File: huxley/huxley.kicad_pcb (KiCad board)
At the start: 2 copper layers, 2 parts, among them U6 NVT2010PW_118

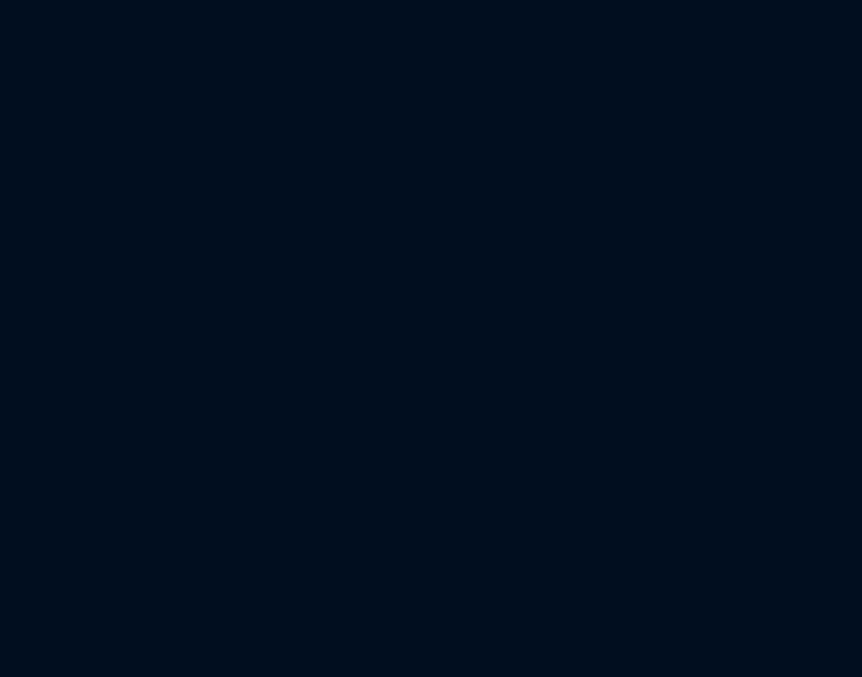
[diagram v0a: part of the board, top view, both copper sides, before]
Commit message: added analog chip schematics and connector footprints
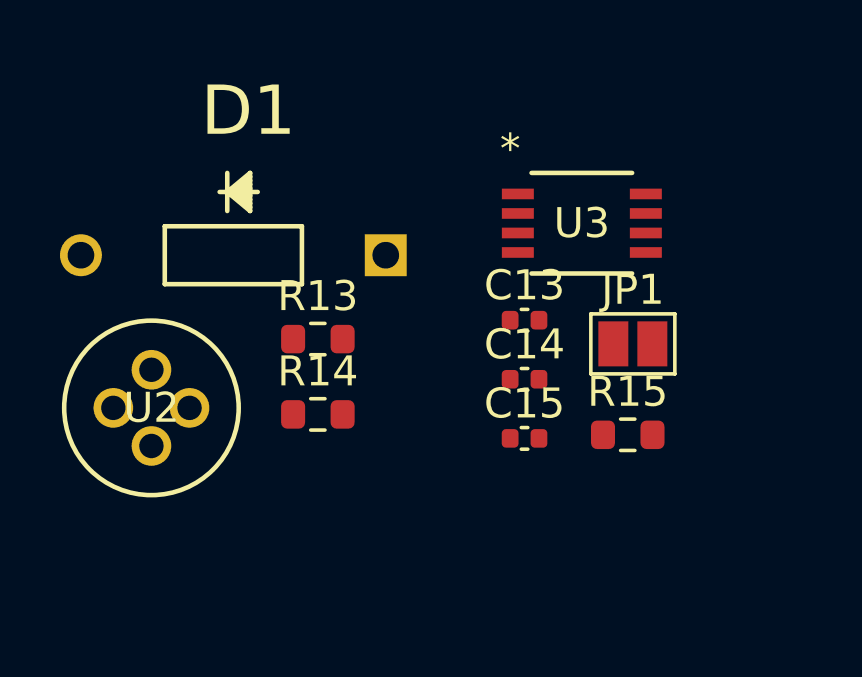
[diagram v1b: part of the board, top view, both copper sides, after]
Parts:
- added C13: 0.1u, Capacitor_SMD:C_0402_1005Metric, F.Cu at (50.2, 36.7)
- added C14: 1n, Capacitor_SMD:C_0402_1005Metric, F.Cu at (50.2, 38.6)
- added C15: 10p, Capacitor_SMD:C_0402_1005Metric, F.Cu at (50.2, 40.6)
- added D1: 1N457, 726_footprints:DIO_1N457, F.Cu at (45.6, 34.5)
- added JP1: Jumper_2_Open, Jumper:SolderJumper-2_P1.3mm_Open_Pad1.0x1.5mm, F.Cu at (53.8, 37.5)
- added R13: 1.59k, Resistor_SMD:R_0603_1608Metric, F.Cu at (43.3, 37.3)
- added R14: 15.9k, Resistor_SMD:R_0603_1608Metric, F.Cu at (43.3, 39.8)
- added R15: 500, Resistor_SMD:R_0603_1608Metric, F.Cu at (53.7, 40.5)
- added U2: LM134H, 726_footprints:lm134, F.Cu at (37.8, 40.9)
- added U3: MAX40201FAUA+, 726_footprints:MAX40201FAUA+, F.Cu at (52.1, 33.4)

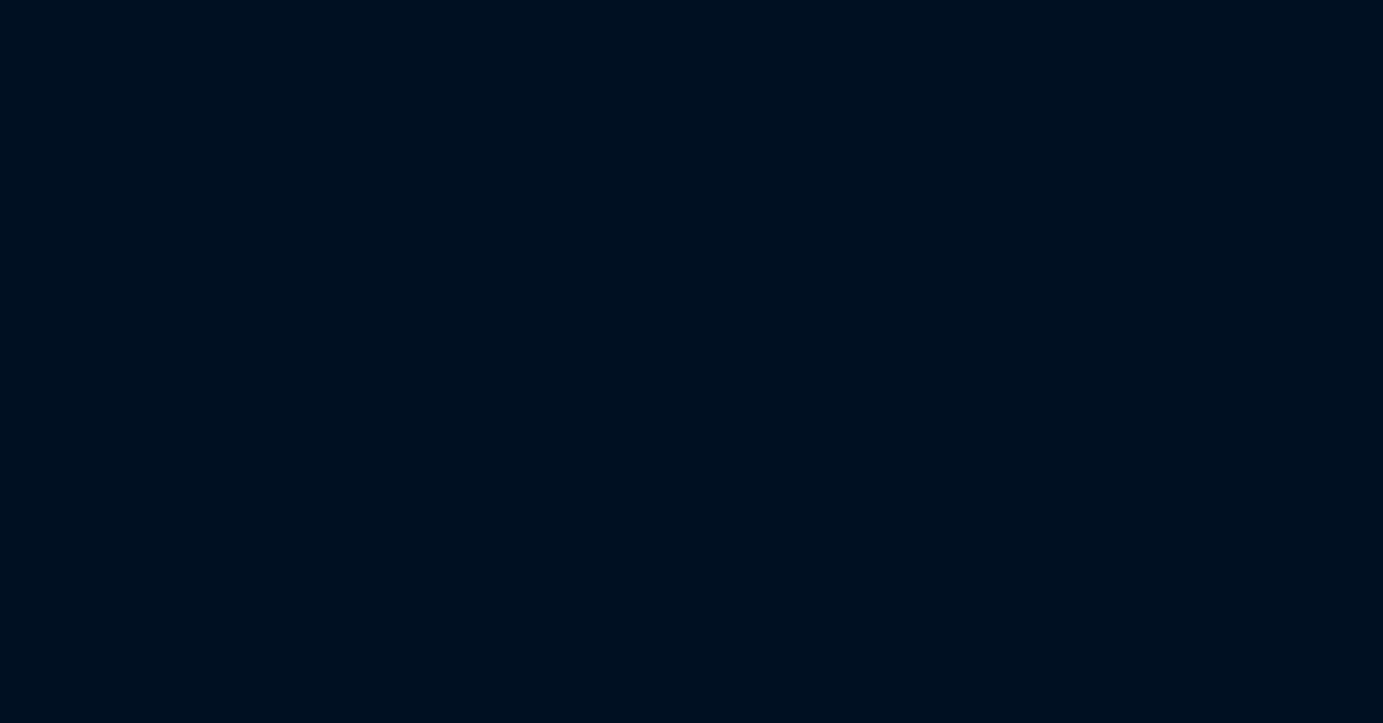
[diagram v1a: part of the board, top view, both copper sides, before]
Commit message: updated Ibias gen and footprints
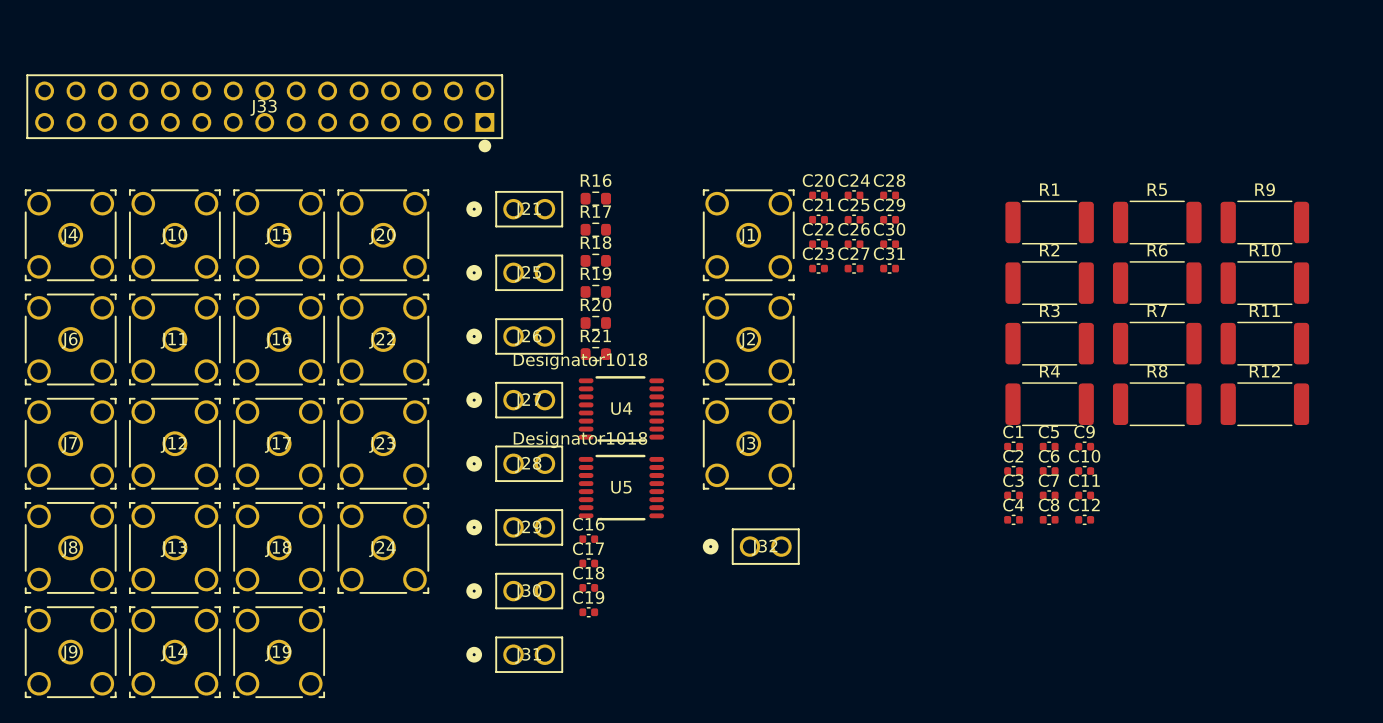
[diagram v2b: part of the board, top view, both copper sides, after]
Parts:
- added C1: 3.19pF, Capacitor_SMD:C_0402_1005Metric, F.Cu at (110.2, 145.9)
- added C10: 3.19pF, Capacitor_SMD:C_0402_1005Metric, F.Cu at (116.0, 147.9)
- added C11: 3.19pF, Capacitor_SMD:C_0402_1005Metric, F.Cu at (116.0, 149.9)
- added C12: 3.19pF, Capacitor_SMD:C_0402_1005Metric, F.Cu at (116.0, 151.8)
- added C16: 0.1u, Capacitor_SMD:C_0402_1005Metric, F.Cu at (75.9, 153.4)
- added C17: 10u, Capacitor_SMD:C_0402_1005Metric, F.Cu at (75.9, 155.4)
- added C18: 10u, Capacitor_SMD:C_0402_1005Metric, F.Cu at (75.9, 157.3)
- added C19: 0.1u, Capacitor_SMD:C_0402_1005Metric, F.Cu at (75.9, 159.3)
- added C2: 3.19pF, Capacitor_SMD:C_0402_1005Metric, F.Cu at (110.2, 147.9)
- added C20: 10u, Capacitor_SMD:C_0402_1005Metric, F.Cu at (94.5, 125.6)
- added C21: 0.1u, Capacitor_SMD:C_0402_1005Metric, F.Cu at (94.5, 127.6)
- added C22: 1n, Capacitor_SMD:C_0402_1005Metric, F.Cu at (94.5, 129.6)
- added C23: 10p, Capacitor_SMD:C_0402_1005Metric, F.Cu at (94.5, 131.5)
- added C24: 10u, Capacitor_SMD:C_0402_1005Metric, F.Cu at (97.4, 125.6)
- added C25: 0.1u, Capacitor_SMD:C_0402_1005Metric, F.Cu at (97.4, 127.6)
- added C26: 1n, Capacitor_SMD:C_0402_1005Metric, F.Cu at (97.4, 129.6)
- added C27: 10p, Capacitor_SMD:C_0402_1005Metric, F.Cu at (97.4, 131.5)
- added C28: 10u, Capacitor_SMD:C_0402_1005Metric, F.Cu at (100.2, 125.6)
- added C29: 0.1u, Capacitor_SMD:C_0402_1005Metric, F.Cu at (100.2, 127.6)
- added C3: 3.19pF, Capacitor_SMD:C_0402_1005Metric, F.Cu at (110.2, 149.9)
- added C30: 1n, Capacitor_SMD:C_0402_1005Metric, F.Cu at (100.2, 129.6)
- added C31: 10p, Capacitor_SMD:C_0402_1005Metric, F.Cu at (100.2, 131.5)
- added C4: 3.19pF, Capacitor_SMD:C_0402_1005Metric, F.Cu at (110.2, 151.8)
- added C5: 3.19pF, Capacitor_SMD:C_0402_1005Metric, F.Cu at (113.1, 145.9)
- added C6: 3.19pF, Capacitor_SMD:C_0402_1005Metric, F.Cu at (113.1, 147.9)
- added C7: 3.19pF, Capacitor_SMD:C_0402_1005Metric, F.Cu at (113.1, 149.9)
- added C8: 3.19pF, Capacitor_SMD:C_0402_1005Metric, F.Cu at (113.1, 151.8)
- added C9: 3.19pF, Capacitor_SMD:C_0402_1005Metric, F.Cu at (116.0, 145.9)
- added J1: SMA_RF2-04A-T-00-50-G, 726_footprints:CONN_RF2-04A-T-00-50-G_ADM, F.Cu at (88.9, 128.9)
- added J10: SMA_RF2-04A-T-00-50-G, 726_footprints:CONN_RF2-04A-T-00-50-G_ADM, F.Cu at (42.5, 128.9)
- added J11: SMA_RF2-04A-T-00-50-G, 726_footprints:CONN_RF2-04A-T-00-50-G_ADM, F.Cu at (42.5, 137.3)
- added J12: SMA_RF2-04A-T-00-50-G, 726_footprints:CONN_RF2-04A-T-00-50-G_ADM, F.Cu at (42.5, 145.7)
- added J13: SMA_RF2-04A-T-00-50-G, 726_footprints:CONN_RF2-04A-T-00-50-G_ADM, F.Cu at (42.5, 154.1)
- added J14: SMA_RF2-04A-T-00-50-G, 726_footprints:CONN_RF2-04A-T-00-50-G_ADM, F.Cu at (42.5, 162.5)
- added J15: SMA_RF2-04A-T-00-50-G, 726_footprints:CONN_RF2-04A-T-00-50-G_ADM, F.Cu at (50.9, 128.9)
- added J16: SMA_RF2-04A-T-00-50-G, 726_footprints:CONN_RF2-04A-T-00-50-G_ADM, F.Cu at (50.9, 137.3)
- added J17: SMA_RF2-04A-T-00-50-G, 726_footprints:CONN_RF2-04A-T-00-50-G_ADM, F.Cu at (50.9, 145.7)
- added J18: SMA_RF2-04A-T-00-50-G, 726_footprints:CONN_RF2-04A-T-00-50-G_ADM, F.Cu at (50.9, 154.1)
- added J19: SMA_RF2-04A-T-00-50-G, 726_footprints:CONN_RF2-04A-T-00-50-G_ADM, F.Cu at (50.9, 162.5)
- added J2: SMA_RF2-04A-T-00-50-G, 726_footprints:CONN_RF2-04A-T-00-50-G_ADM, F.Cu at (88.9, 137.3)
- added J20: SMA_RF2-04A-T-00-50-G, 726_footprints:CONN_RF2-04A-T-00-50-G_ADM, F.Cu at (59.3, 128.9)
- added J21: 61300211121, 726_footprints:CONN_61300211121_WRE, F.Cu at (69.9, 126.8)
- added J22: SMA_RF2-04A-T-00-50-G, 726_footprints:CONN_RF2-04A-T-00-50-G_ADM, F.Cu at (59.3, 137.3)
- added J23: SMA_RF2-04A-T-00-50-G, 726_footprints:CONN_RF2-04A-T-00-50-G_ADM, F.Cu at (59.3, 145.7)
- added J24: SMA_RF2-04A-T-00-50-G, 726_footprints:CONN_RF2-04A-T-00-50-G_ADM, F.Cu at (59.3, 154.1)
- added J25: 61300211121, 726_footprints:CONN_61300211121_WRE, F.Cu at (69.9, 131.9)
- added J26: 61300211121, 726_footprints:CONN_61300211121_WRE, F.Cu at (69.9, 137.0)
- added J27: 61300211121, 726_footprints:CONN_61300211121_WRE, F.Cu at (69.9, 142.2)
- added J28: 61300211121, 726_footprints:CONN_61300211121_WRE, F.Cu at (69.9, 147.3)
- added J29: 61300211121, 726_footprints:CONN_61300211121_WRE, F.Cu at (69.9, 152.5)
- added J3: SMA_RF2-04A-T-00-50-G, 726_footprints:CONN_RF2-04A-T-00-50-G_ADM, F.Cu at (88.9, 145.7)
- added J30: 61300211121, 726_footprints:CONN_61300211121_WRE, F.Cu at (69.9, 157.6)
- added J31: 61300211121, 726_footprints:CONN_61300211121_WRE, F.Cu at (69.9, 162.7)
- added J32: 61300211121, 726_footprints:CONN_61300211121_WRE, F.Cu at (89.0, 154.0)
- added J33: 67996-130HLF, 726_footprints:30p_connector, F.Cu at (67.6, 119.7)
- added J4: SMA_RF2-04A-T-00-50-G, 726_footprints:CONN_RF2-04A-T-00-50-G_ADM, F.Cu at (34.1, 128.9)
- added J6: SMA_RF2-04A-T-00-50-G, 726_footprints:CONN_RF2-04A-T-00-50-G_ADM, F.Cu at (34.1, 137.3)
- added J7: SMA_RF2-04A-T-00-50-G, 726_footprints:CONN_RF2-04A-T-00-50-G_ADM, F.Cu at (34.1, 145.7)
- added J8: SMA_RF2-04A-T-00-50-G, 726_footprints:CONN_RF2-04A-T-00-50-G_ADM, F.Cu at (34.1, 154.1)
- added J9: SMA_RF2-04A-T-00-50-G, 726_footprints:CONN_RF2-04A-T-00-50-G_ADM, F.Cu at (34.1, 162.5)
- added R1: 50, Resistor_SMD:R_2512_6332Metric, F.Cu at (113.2, 127.8)
- added R10: 50, Resistor_SMD:R_2512_6332Metric, F.Cu at (130.5, 132.7)
- added R11: 50, Resistor_SMD:R_2512_6332Metric, F.Cu at (130.5, 137.6)
- added R12: 50, Resistor_SMD:R_2512_6332Metric, F.Cu at (130.5, 142.5)
- added R16: 75k, Resistor_SMD:R_0603_1608Metric, F.Cu at (76.5, 125.9)
- added R17: 89.8k, Resistor_SMD:R_0603_1608Metric, F.Cu at (76.5, 128.4)
- added R18: 66.5k, Resistor_SMD:R_0603_1608Metric, F.Cu at (76.5, 130.9)
- added R19: 750k, Resistor_SMD:R_0603_1608Metric, F.Cu at (76.5, 133.4)
- added R2: 50, Resistor_SMD:R_2512_6332Metric, F.Cu at (113.2, 132.7)
- added R20: 898k, Resistor_SMD:R_0603_1608Metric, F.Cu at (76.5, 135.9)
- added R21: 665k, Resistor_SMD:R_0603_1608Metric, F.Cu at (76.5, 138.5)
- added R3: 50, Resistor_SMD:R_2512_6332Metric, F.Cu at (113.2, 137.6)
- added R4: 50, Resistor_SMD:R_2512_6332Metric, F.Cu at (113.2, 142.5)
- added R5: 50, Resistor_SMD:R_2512_6332Metric, F.Cu at (121.8, 127.8)
- added R6: 50, Resistor_SMD:R_2512_6332Metric, F.Cu at (121.8, 132.7)
- added R7: 50, Resistor_SMD:R_2512_6332Metric, F.Cu at (121.8, 137.6)
- added R8: 50, Resistor_SMD:R_2512_6332Metric, F.Cu at (121.8, 142.5)
- added R9: 50, Resistor_SMD:R_2512_6332Metric, F.Cu at (130.5, 127.8)
- added U4: TMUX1112PWR, 726_footprints:TMUX1111PWR, F.Cu at (78.6, 142.9)
- added U5: TMUX1112PWR, 726_footprints:TMUX1111PWR, F.Cu at (78.6, 149.2)
- R13: value 1.59k -> 1.62k
- R14: value 15.9k -> 16.2k
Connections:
- R13 pad 1: Net-(U2-R) -> /ibias/R1_1
- R14 pad 1: Net-(U2-R) -> /ibias/R2_1
- U2 pad 1: Net-(U2-R) -> /ibias/ibias_rset

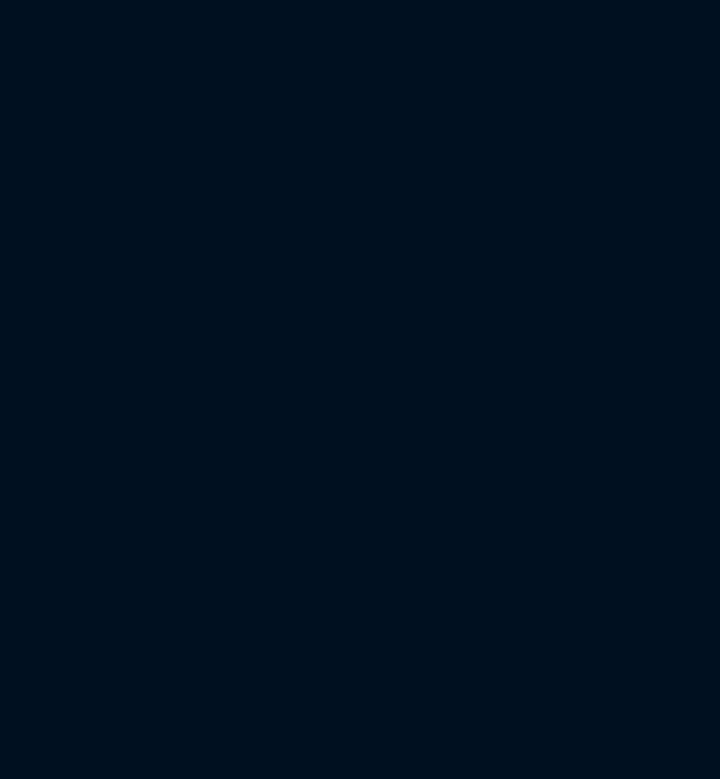
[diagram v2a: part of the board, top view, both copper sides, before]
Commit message: updated footprints
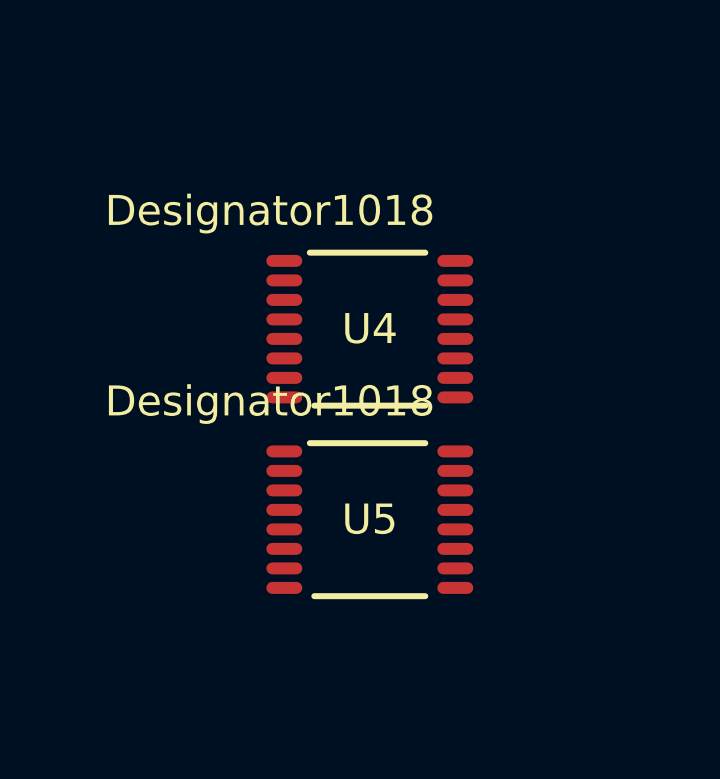
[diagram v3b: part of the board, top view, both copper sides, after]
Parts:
- added U4: TMUX1112PWR, 726_footprints:TMUX1111PWR, F.Cu at (40.7, 58.4)
- added U5: TMUX1112PWR, 726_footprints:TMUX1111PWR, F.Cu at (40.7, 64.7)
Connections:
- J1 pad 2: (no net) -> GND
- J10 pad 2: (no net) -> GND
- J11 pad 2: (no net) -> GND
- J12 pad 2: (no net) -> GND
- J13 pad 2: (no net) -> GND
- J14 pad 2: (no net) -> GND
- J15 pad 2: (no net) -> GND
- J16 pad 2: (no net) -> GND
- J17 pad 2: (no net) -> GND
- J18 pad 2: (no net) -> GND
- J19 pad 1: unconnected-(J19-Pad1) -> vd1_dummy
- J19 pad 2: (no net) -> GND
- J19 pad 3: Net-(J19-Ext-Pad3) -> GND
- J19 pad 4: Net-(J19-Ext-Pad3) -> GND
- J19 pad 5: Net-(J19-Ext-Pad3) -> GND
- J2 pad 2: (no net) -> GND
- J20 pad 2: (no net) -> GND
- J22 pad 2: (no net) -> GND
- J23 pad 2: (no net) -> GND
- J24 pad 2: (no net) -> GND
- J3 pad 2: (no net) -> GND
- J4 pad 2: (no net) -> GND
- J6 pad 2: (no net) -> GND
- J7 pad 2: (no net) -> GND
- J8 pad 2: (no net) -> GND
- J9 pad 2: (no net) -> GND

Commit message: layout
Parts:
- removed JP1: Jumper_2_Open, Jumper:SolderJumper-2_P1.3mm_Open_Pad1.0x1.5mm
- removed the U4 at (78.6, 142.9)
- removed the U5 at (78.6, 149.2)
- added C32: 10u, Capacitor_SMD:C_0402_1005Metric, F.Cu at (131.0, 122.2)
- added C33: 0.1u, Capacitor_SMD:C_0402_1005Metric, F.Cu at (129.0, 122.2)
- added C34: 1n, Capacitor_SMD:C_0402_1005Metric, F.Cu at (127.1, 122.2)
- added C35: 10p, Capacitor_SMD:C_0402_1005Metric, F.Cu at (125.1, 122.2)
- added C36: 10u, Capacitor_SMD:C_0402_1005Metric, F.Cu at (143.0, 33.6)
- added C37: 0.1u, Capacitor_SMD:C_0402_1005Metric, F.Cu at (143.0, 35.6)
- added C38: 1n, Capacitor_SMD:C_0402_1005Metric, F.Cu at (143.0, 37.6)
- added C39: 10p, Capacitor_SMD:C_0402_1005Metric, F.Cu at (143.0, 39.5)
- added C40: 10u, Capacitor_SMD:C_0402_1005Metric, F.Cu at (143.0, 41.5)
- added C41: 0.1u, Capacitor_SMD:C_0402_1005Metric, F.Cu at (143.0, 43.5)
- added C42: 1n, Capacitor_SMD:C_0402_1005Metric, F.Cu at (143.0, 45.4)
- added C43: 10p, Capacitor_SMD:C_0402_1005Metric, F.Cu at (143.0, 47.4)
- added J5: SMA_RF2-04A-T-00-50-G, 726_footprints:CONN_RF2-04A-T-00-50-G_ADM, F.Cu at (64.4, 59.1)
- moved J9 152.8 mm to (153.1, 66.6)
- moved J10 133.0 mm to (153.3, 55.3)
- moved C16 130.6 mm to (126.5, 33.0)
- moved C17 130.6 mm to (126.5, 35.0)
- moved J31 128.8 mm to (111.8, 41.0)
- moved C18 124.6 mm to (78.0, 32.8)
- moved C19 124.6 mm to (78.0, 34.8)
- moved J8 123.4 mm to (138.8, 88.8)
- moved J18 120.3 mm to (125.1, 59.3)
- moved J30 119.9 mm to (97.7, 41.0)
- moved J7 115.7 mm to (138.9, 96.8)
- moved J3 114.1 mm to (38.3, 43.4)
- moved C30 112.8 mm to (38.0, 35.5)
- moved C31 112.8 mm to (38.0, 37.5)
- moved C28 112.8 mm to (38.0, 31.6)
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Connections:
- C16 pad 1: PP_VDDIO_1V8 -> PP_TAVDD_1V8
- C17 pad 1: PP_VDDIO_1V8 -> PP_TAVDD_1V8
- C18 pad 1: PP_VDDIO_1V8 -> PP_TAVDD_1V8
- C19 pad 1: PP_VDDIO_1V8 -> PP_TAVDD_1V8
- U4 pad 13: PP_VDDIO_1V8 -> PP_TAVDD_1V8
- U5 pad 13: PP_VDDIO_1V8 -> PP_TAVDD_1V8
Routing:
- net PP_TAVDD_1V8: track 0.00 -> 58.9 mm
- net +3.3V: track 0.00 -> 18.4 mm
- net PP_VDDIO_1V8: track 0.00 -> 13.8 mm
- net vbias2: track 0.00 -> 5.92 mm
- net GND: track 0.00 -> 3.15 mm, vias 0 -> 59
- net Net-(D1-A): track 0.00 -> 1.74 mm
- added copper zone on In1.Cu, net GND
- added copper zone on In2.Cu, net PP_TAVDD_1V8
- added copper zone on In2.Cu, net PP_VDDIO_1V8
- added copper zone on In2.Cu, net PP_VDD_0V9
- added copper zone on B.Cu, net vlvl
- added copper zone on B.Cu, net vrbias
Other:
- copper layers 2 -> 4
- board text added: "output_2a"
- board text added: "output_2b"

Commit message: layout_1
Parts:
- moved J33 2.46 mm to (81.2, 131.8)
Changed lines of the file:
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@@
 		(fp_arc
 			(start 2.199991 2.300016)
-			(mid 2.141414 2.44144)
+			(mid 2.141413 2.441437)
 			(end 1.999991 2.500015)
 			(stroke
@@
 		(fp_arc
 			(start 2.199991 2.300016)
-			(mid 2.141414 2.44144)
+			(mid 2.141413 2.441437)
 			(end 1.999991 2.500015)
 			(stroke
@@
 	(footprint "726_footprints:30p_connector"
 		(layer "F.Cu")
-		(at 78.75 131.75 180)
+		(at 81.21 131.75 180)
 		(tags "67996-130HLF ")
 		(property "Reference" "J33"
